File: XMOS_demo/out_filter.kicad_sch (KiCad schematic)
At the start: 0 parts

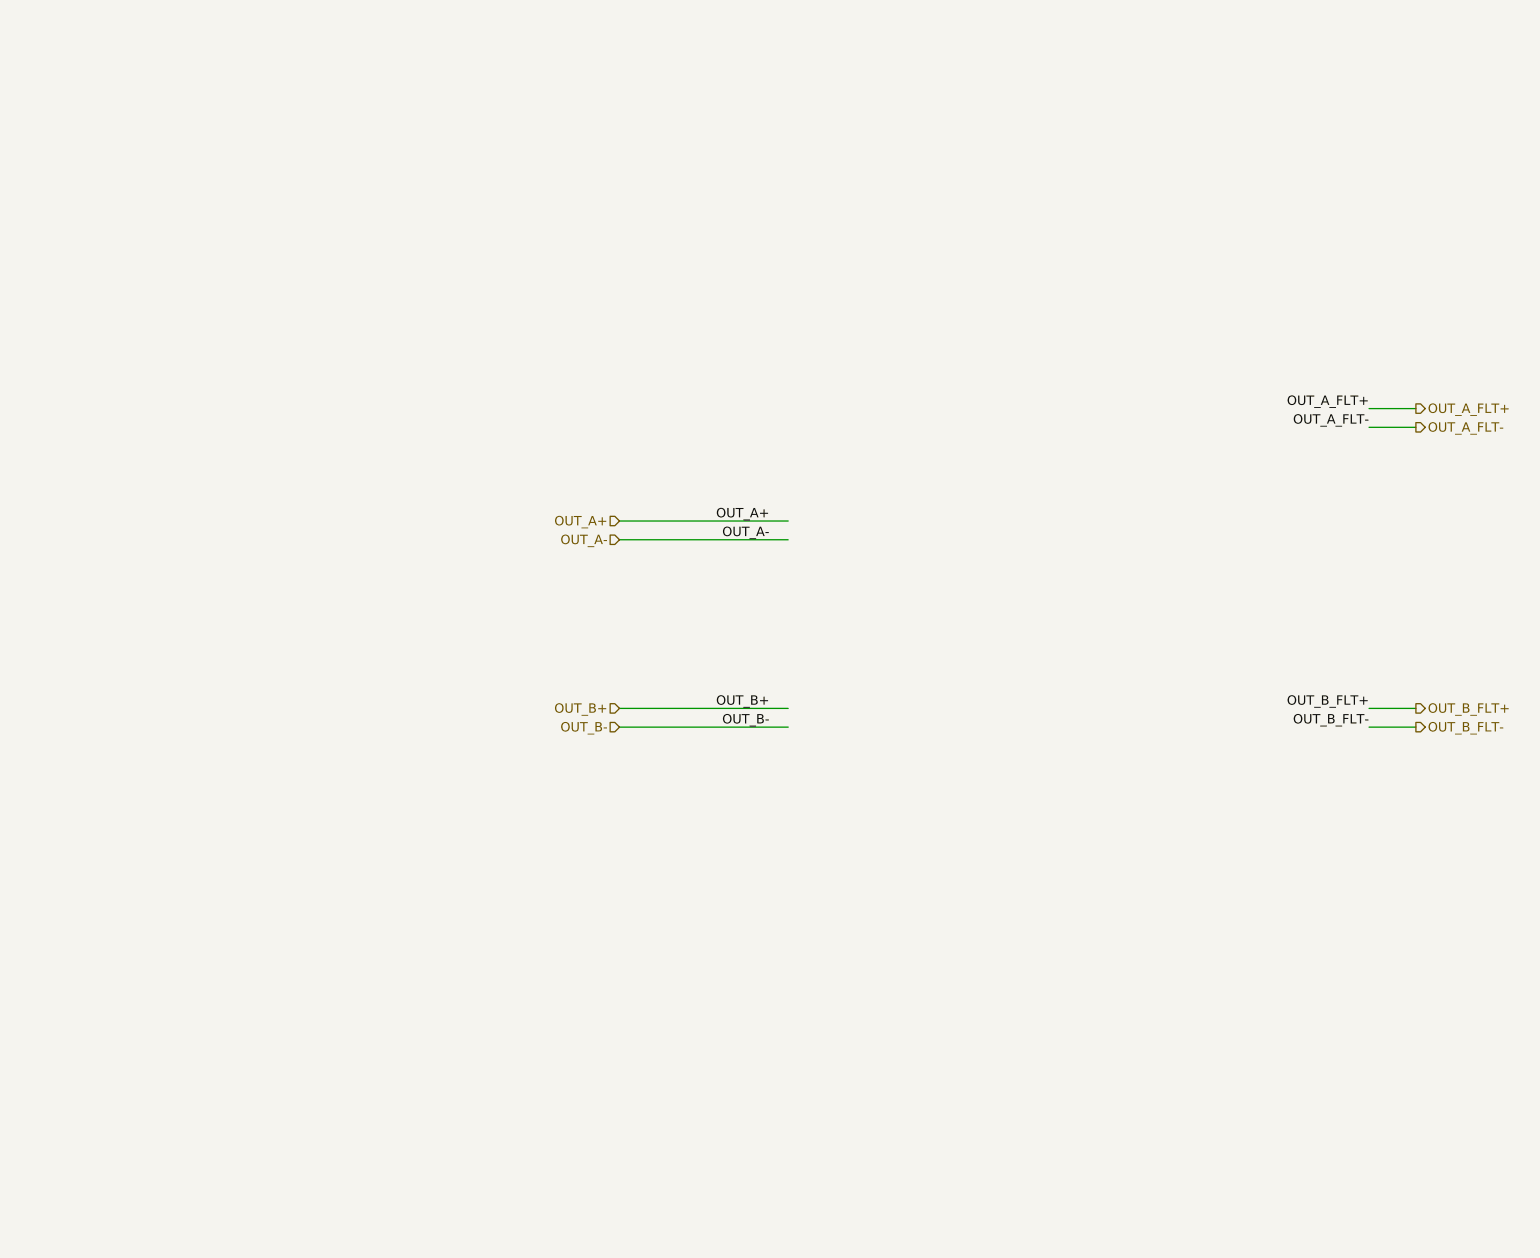
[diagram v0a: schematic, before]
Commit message: Updated sch and pcb with active filter
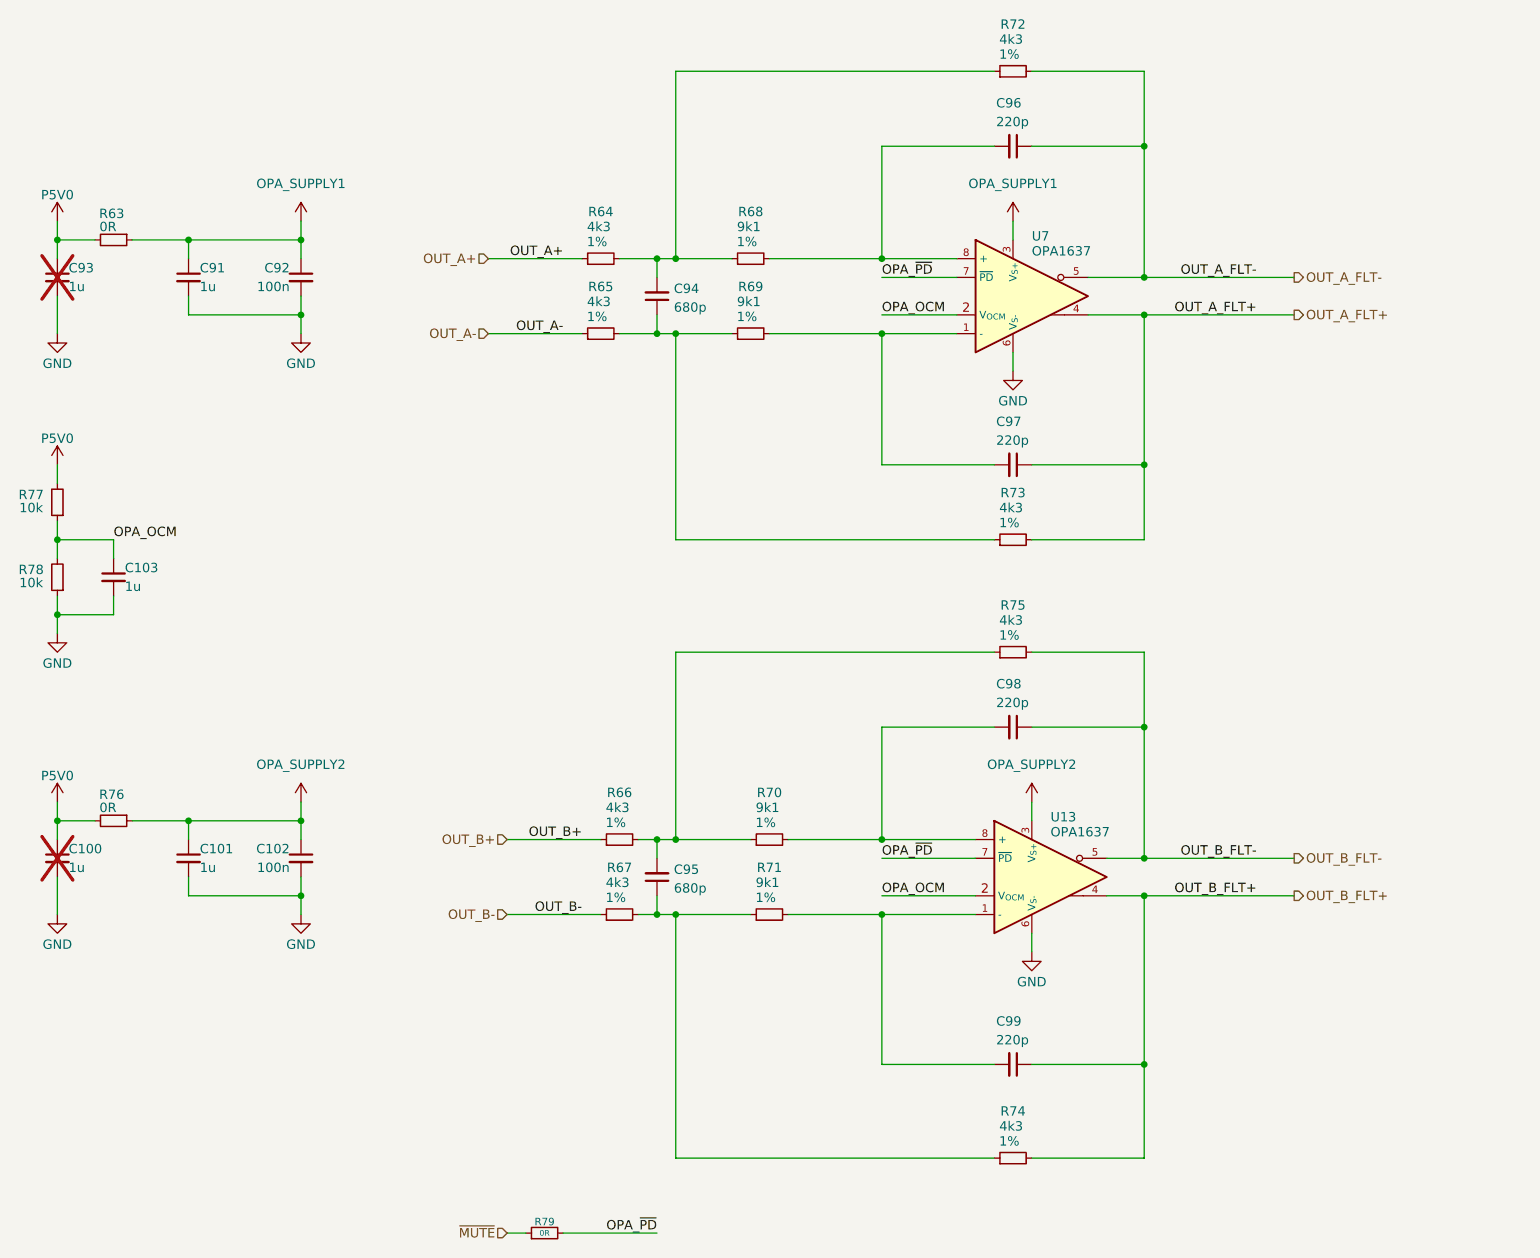
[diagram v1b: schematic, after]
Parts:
- added C100, C101, C103, C91, C93: 1u, Capacitor_SMD:C_0603_1608Metric, symbol Device:C_Small
- added C102, C92: 100n, Capacitor_SMD:C_0402_1005Metric, symbol Device:C_Small
- added C94, C95: 680p, Capacitor_SMD:C_0603_1608Metric, symbol Device:C_Small
- added C96, C97, C98, C99: 220p, Capacitor_SMD:C_0603_1608Metric, symbol Device:C_Small
- added R63, R76, R79: 0R, Resistor_SMD:R_0603_1608Metric, symbol Device:R_Small
- added R64, R65, R66, R67, R72, R73, R74, R75: 4k3, Resistor_SMD:R_0603_1608Metric, symbol Device:R_Small
- added R68, R69, R70, R71: 9k1, Resistor_SMD:R_0603_1608Metric, symbol Device:R_Small
- added R77, R78: 10k, Resistor_SMD:R_0603_1608Metric, symbol Device:R_Small
- added U13, U7: OPA1637, Package_SO:VSSOP-8_3x3mm_P0.65mm, symbol _Amplifier_Difference:OPA1637
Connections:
- net OUT_A+: now also R64.1
- net OUT_A-: now also R65.1
- net OUT_A_FLT+: now also C97.1, R73.2, U7.4
- net OUT_A_FLT-: now also C96.1, R72.2, U7.5
- net OUT_B+: now also R66.1
- net OUT_B-: now also R67.1
- net OUT_B_FLT+: now also C99.1, R74.2, U13.4
- net OUT_B_FLT-: now also C98.1, R75.2, U13.5
- new net: C95.2, R66.2, R70.1, R75.1
- new net: C98.2, R70.2, U13.8 (+)
- new net: C97.2, R69.2, U7.1 (-)
- new net: C96.2, R68.2, U7.8 (+)
- new net: C95.1, R67.2, R71.1, R74.1
- new net: C94.2, R64.2, R68.1, R72.1
- new net: C99.2, R71.2, U13.1 (-)
- new net: C94.1, R65.2, R69.1, R73.1
- new net GND: C100.2, C101.2, C102.2, C103.2, C91.2, C92.2, C93.2, R78.1, U13.6 (V_{S-}), U7.6 (V_{S-})
- new net OPA_OCM: C103.1, R77.1, R78.2, U13.2 (V_{OCM}), U7.2 (V_{OCM})
- new net OPA_SUPPLY1: C91.1, C92.1, R63.1, U7.3 (V_{S+})
- new net OPA_SUPPLY2: C101.1, C102.1, R76.1, U13.3 (V_{S+})
- new net OPA_~{PD}: R79.2, U13.7 (~{PD}), U7.7 (~{PD})
- new net P5V0: C100.1, C93.1, R63.2, R76.2, R77.2
- new net ~{MUTE}: R79.1
